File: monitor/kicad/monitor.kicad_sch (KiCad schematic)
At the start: 7 parts, among them SW1 SW_Push, SW2 SW_Push, SW3 SW_Push, SW4 SW_Push, U1 SensorSoilMoisture

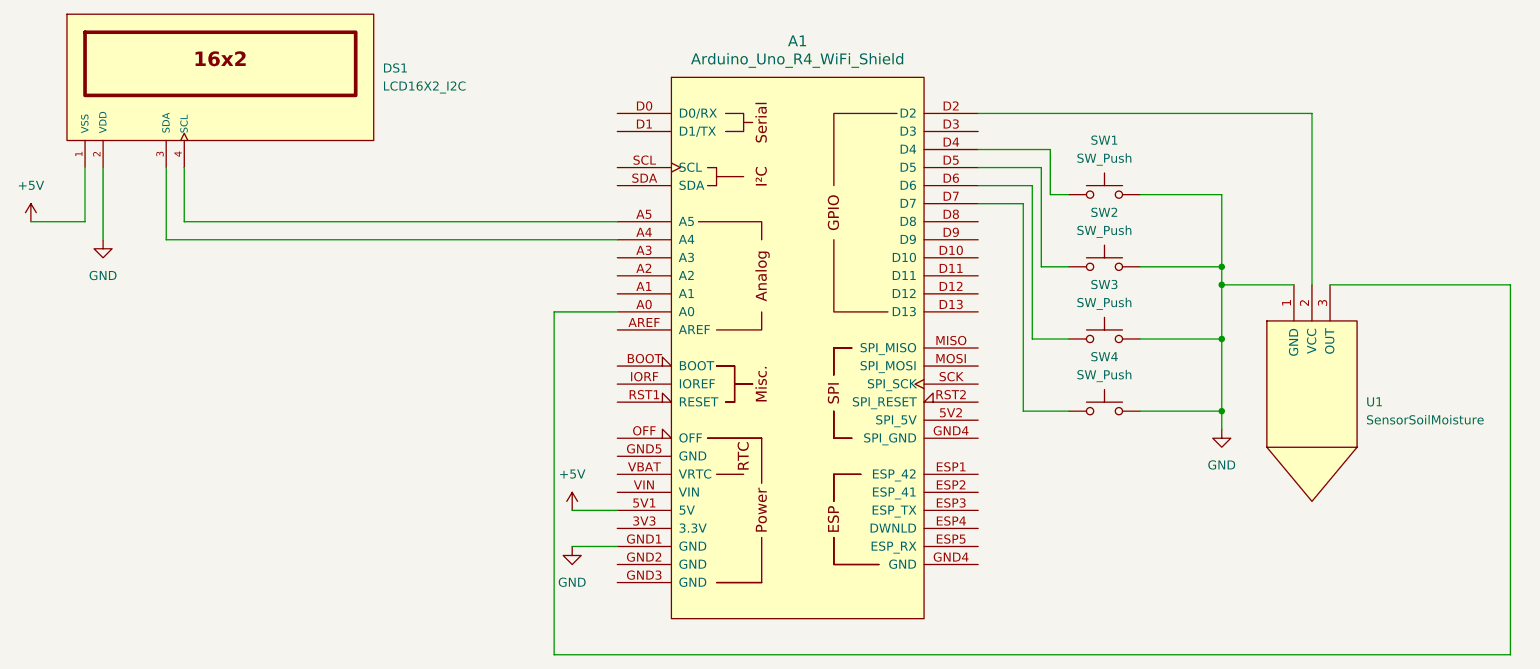
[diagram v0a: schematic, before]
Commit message: Monitor v1.2-v1.4: Configurable parameters, memory optimization, and DIS pin control
This commit includes three unreleased versions (v1.2, v1.3, v1.4):

v1.2: Configurable sensor parameters
- Add Settings menu for backlight timeout, sensor warmup, num measurements, delay
- Add min/max ADC tracking in CSV export
- Entry size: 4 → 8 bytes, capacity: 1,344 → 672 entries

v1.3: Memory optimization
- Remove min/max ADC from EEPROM storage (saves 4 bytes per entry)
- Entry size: 8 → 4 bytes, capacity: 672 → 1,344 entries (14 days)
- Min/max still shown in live Serial Monitor output

v1.4: DIS pin control for sensor power management
- Switch from VCC GPIO power cycling to DIS pin GPIO control
- Sensor VCC connects to 5V (constant power), D2 controls DIS pin
- Invert logic: HIGH=disabled, LOW=enabled
- Reduce warmup time: 1000ms → 500ms

⚠️ BREAKING CHANGE (v1.4): Hardware migration required
- Sensor VCC: D2 → 5V
- Sensor DIS: GND → D2

Updated: firmware, README, CHANGELOG, BOM, CLAUDE.md, KiCad schematic
POC variant unchanged (still uses VCC switching)

🤖 Generated with [Claude Code](https://claude.com/claude-code)

Co-Authored-By: Claude <noreply@anthropic.com>
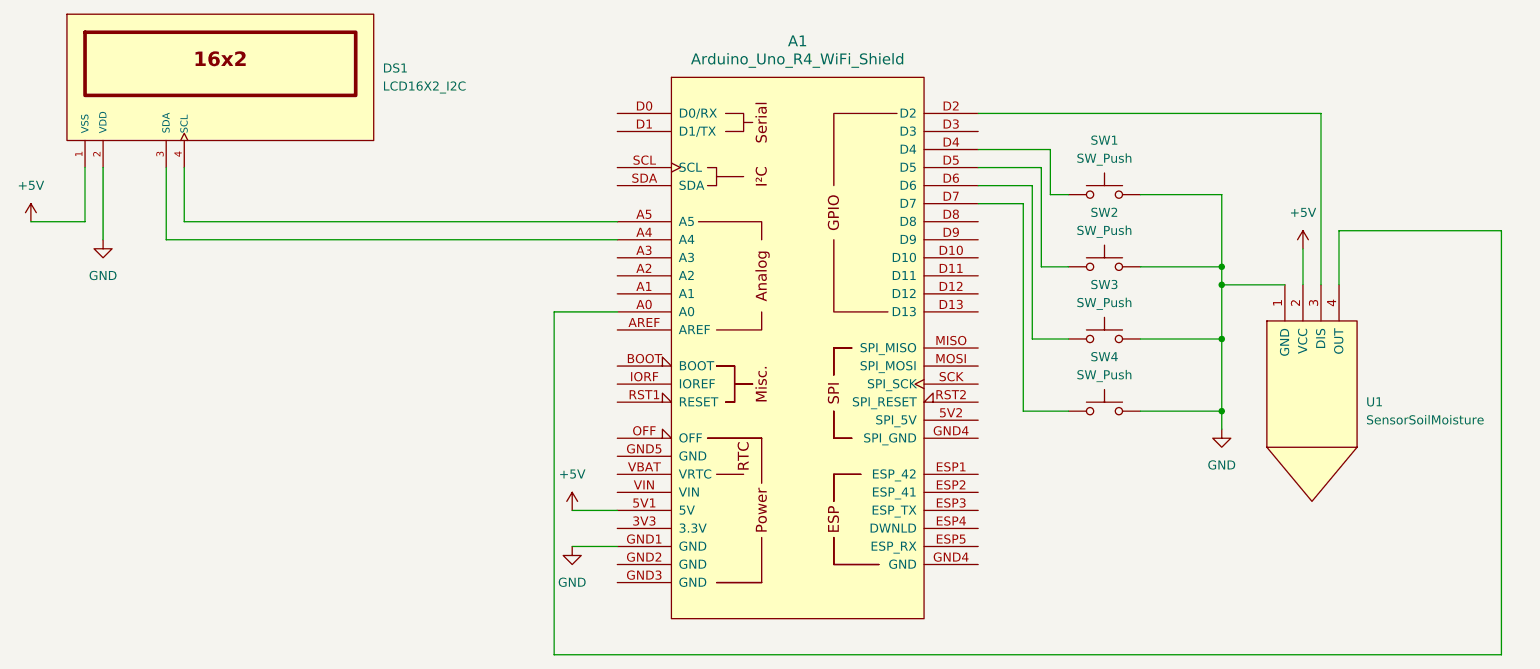
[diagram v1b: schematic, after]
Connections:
- net +5V: now also U1.2 (VCC)
- net at A1.D2: now also U1.3 (DIS); no longer U1.2 (VCC)
- net at A1.A0: now also U1.4 (OUT); no longer U1.3 (OUT)
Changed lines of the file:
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@@
+	(wire
+		(pts
+			(xy 215.9 58.42) (xy 215.9 82.55)
+		)
+		(stroke
+			(width 0)
+			(type default)
+		)
+	)
 	(wire
 		(pts
@@
 	(wire
 		(pts
+			(xy 218.44 74.93) (xy 218.44 82.55)
+		)
+		(stroke
+			(width 0)
+			(type default)
+		)
+	)
+	(wire
+		(pts
 			(xy 107.95 134.62) (xy 107.95 86.36)
 		)
@@
 	(wire
 		(pts
+			(xy 167.64 58.42) (xy 215.9 58.42)
+		)
+		(stroke
+			(width 0)
+			(type default)
+		)
+	)
+	(wire
+		(pts
 			(xy 190.5 69.85) (xy 201.93 69.85)
 		)
@@
 	(wire
 		(pts
-			(xy 217.17 82.55) (xy 242.57 82.55)
+			(xy 218.44 74.93) (xy 241.3 74.93)
 		)
 		(stroke
@@
 	(wire
 		(pts
-			(xy 242.57 82.55) (xy 242.57 134.62)
+			(xy 241.3 74.93) (xy 241.3 134.62)
 		)
 		(stroke
@@
 	(wire
 		(pts
-			(xy 242.57 134.62) (xy 107.95 134.62)
+			(xy 241.3 134.62) (xy 107.95 134.62)
 		)
 		(stroke
@@
 	(wire
 		(pts
-			(xy 214.63 58.42) (xy 214.63 82.55)
-		)
-		(stroke
-			(width 0)
-			(type default)
-		)
-	)
-	(wire
-		(pts
 			(xy 177.8 69.85) (xy 177.8 63.5)
 		)
@@
 	(wire
 		(pts
-			(xy 167.64 58.42) (xy 214.63 58.42)
+			(xy 213.36 77.47) (xy 213.36 82.55)
 		)
 		(stroke
@@
 	(wire
 		(pts
-			(xy 212.09 82.55) (xy 201.93 82.55)
+			(xy 210.82 82.55) (xy 201.93 82.55)
 		)
 		(stroke
@@
 		(pin "1"
 		)
+		(pin "4"
+		)
 		(instances
 			(project ""
@@
 					(unit 1)
 				)
+			)
+		)
+	)
+	(symbol
+		(lib_id "power:+5V")
+		(at 213.36 77.47 0)
+		(unit 1)
+		(exclude_from_sim no)
+		(in_bom yes)
+		(on_board yes)
+		(dnp no)
+		(fields_autoplaced yes)
+		(property "Reference" "#PWR06"
+			(at 213.36 81.28 0)
+			(effects
+				(font
+					(size 1.27 1.27)
+				)
+				(hide yes)
+			)
+		)
+		(property "Value" "+5V"
+			(at 213.36 72.39 0)
+			(effects
+				(font
+					(size 1.27 1.27)
+				)
+			)
+		)
+		(property "Footprint" ""
+			(at 213.36 77.47 0)
+			(effects
+				(font
+					(size 1.27 1.27)
+				)
+				(hide yes)
+			)
+		)
+		(property "Datasheet" ""
+			(at 213.36 77.47 0)
+			(effects
+				(font
+					(size 1.27 1.27)
+				)
+				(hide yes)
+			)
+		)
+		(property "Description" "Power symbol creates a global label with name \"+5V\""
+			(at 213.36 77.47 0)
+			(effects
+				(font
+					(size 1.27 1.27)
+				)
+				(hide yes)
+			)
+		)
+		(pin "1"
+		)
+		(instances
+			(project "monitor"
+				(path "/808532ee-7c15-424a-9c20-bb44fb0ddf6e"
+					(reference "#PWR06")
+					(unit 1)
+				)
